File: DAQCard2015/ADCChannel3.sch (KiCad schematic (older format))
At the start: 21 parts, among them U8 THS4524IDBTR, U9 AD9219

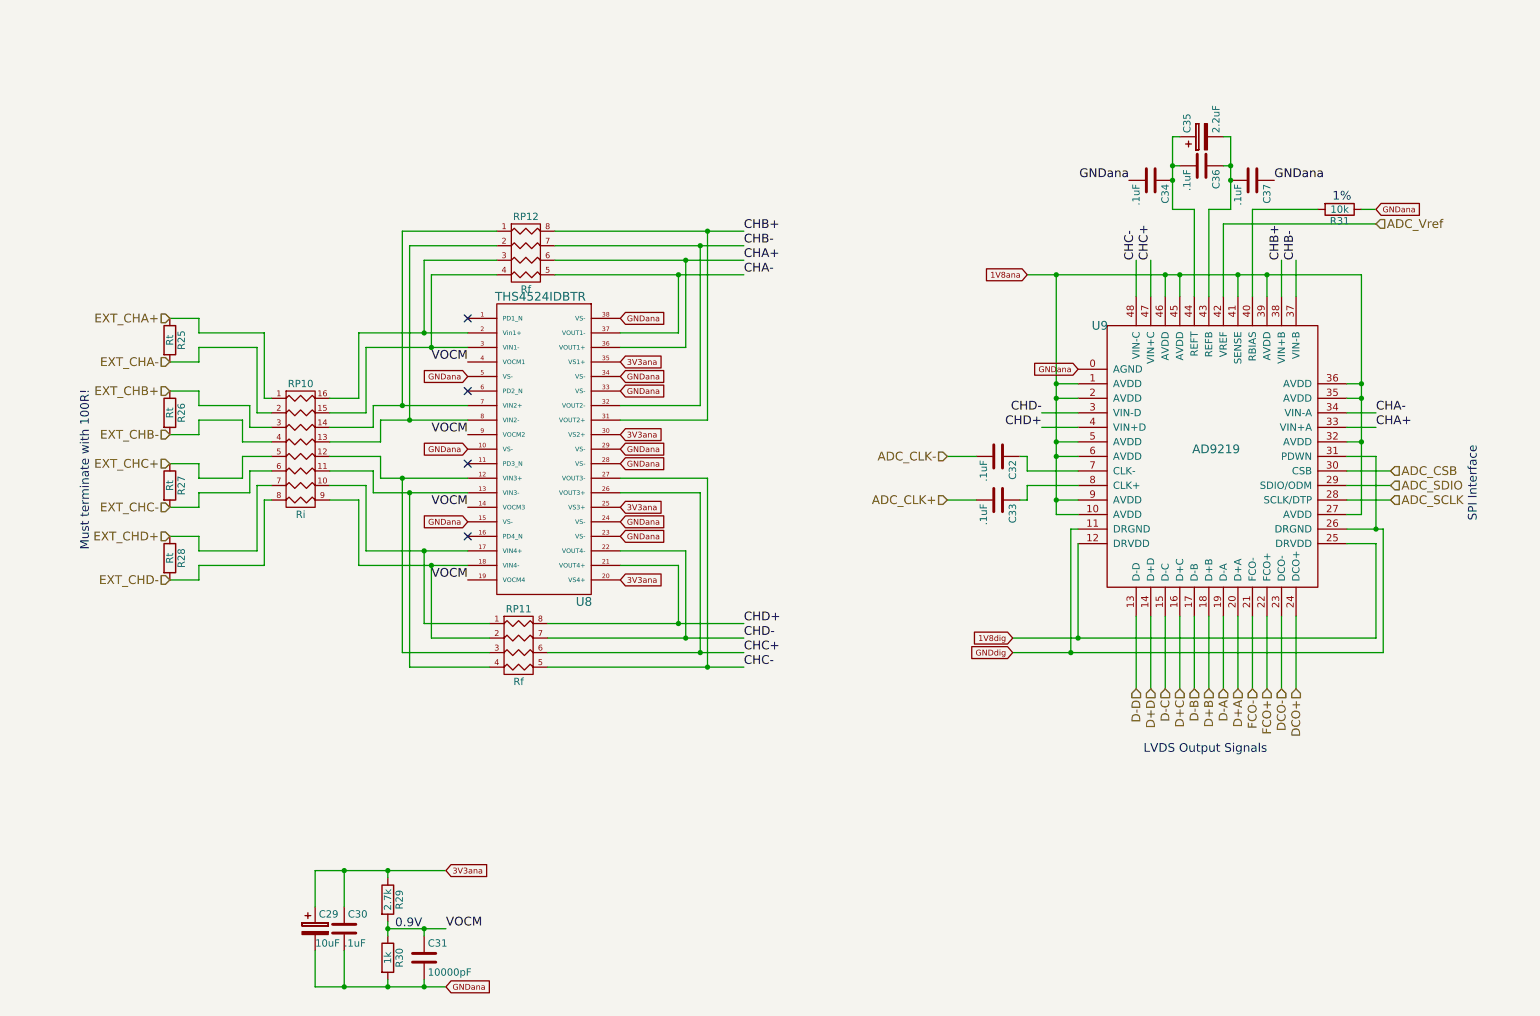
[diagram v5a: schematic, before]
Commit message: propogate previous changes to other channels and schematic
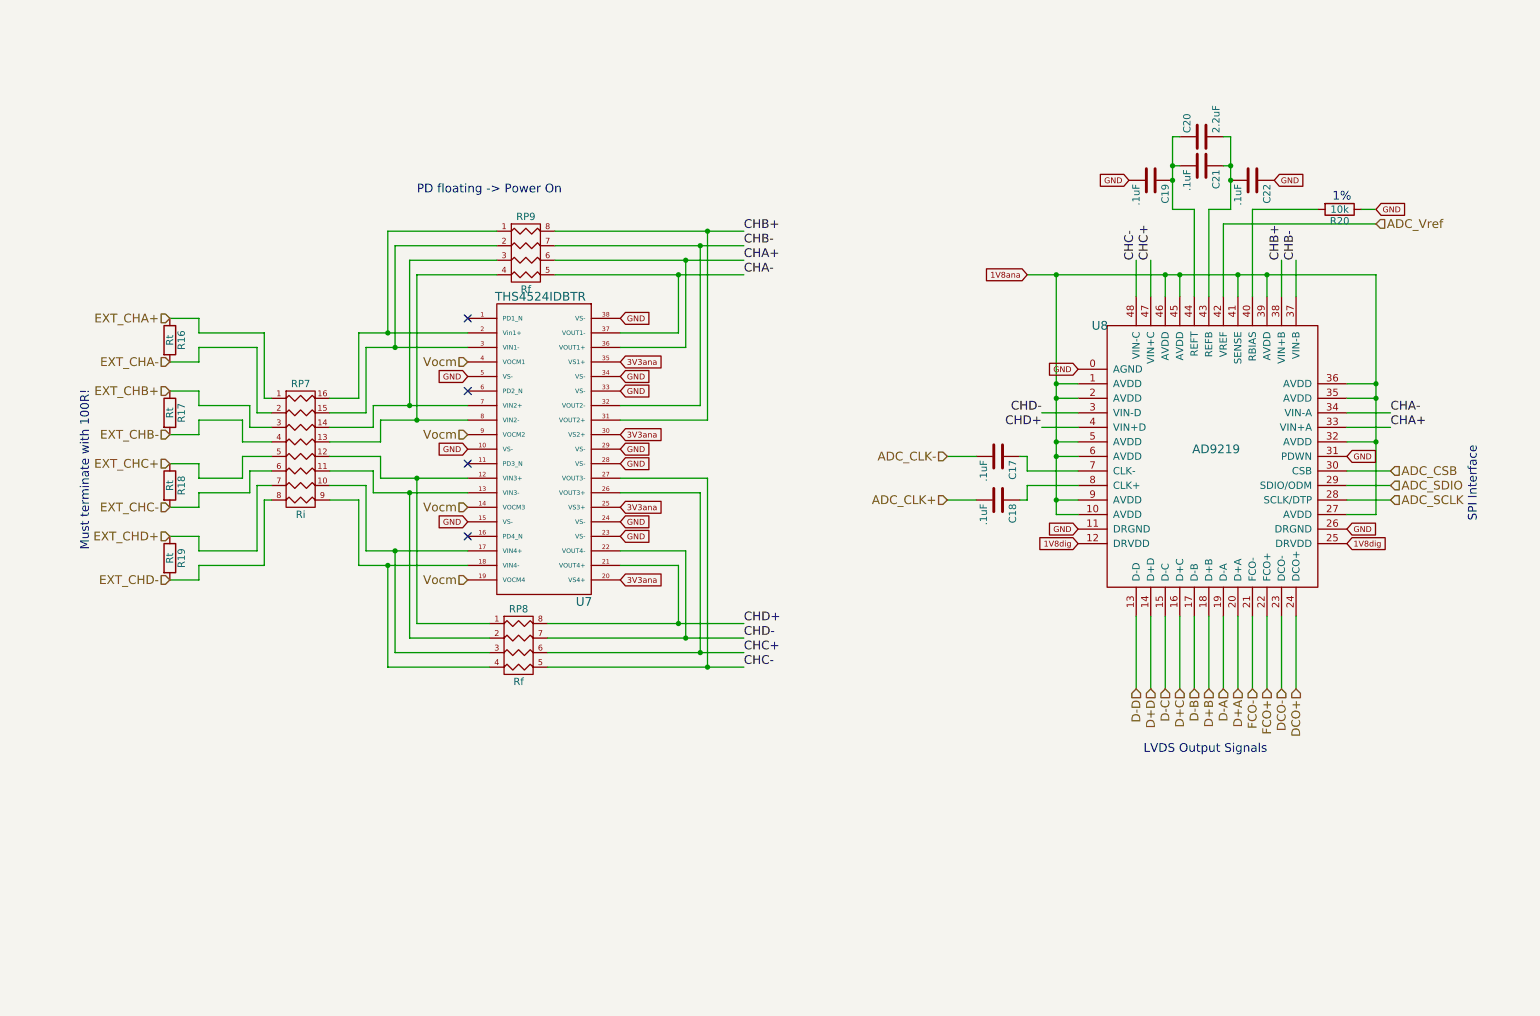
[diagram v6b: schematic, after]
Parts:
- removed C29: 10uF, Capacitors_SMD:C_0805, symbol CP
- removed C30, C32, C33, C34, C36, C37: .1uF, Capacitors_SMD:C_0603, symbol C
- removed C31: 10000pF, Capacitors_SMD:C_0603, symbol C
- removed C35: 2.2uF, Capacitors_SMD:C_0805, symbol CP
- removed R25, R26, R27, R28: Rt, Resistors_SMD:R_0603, symbol R
- removed R29: 2.7k, Resistors_SMD:R_0603, symbol R
- removed R30: 1k, Resistors_SMD:R_0603, symbol R
- removed R31: 10k, Resistors_SMD:R_0603, symbol R
- removed RP10: Ri, extras:R8_MNR18, symbol R_PACK8
- removed RP11, RP12: Rf, extras:R4-MNR04, symbol R_PACK4
- removed U8: THS4524IDBTR, Housings_SSOP:TSSOP-38_4.4x9.7mm_Pitch0.5mm, symbol THS4524IDBTR
- removed U9: AD9219, SMD_Packages:QFN-48-1EP, symbol AD9219
- added C17, C18, C19, C21, C22: .1uF, Capacitors_SMD:C_0603, symbol C
- added C20: 2.2uF, Capacitors_SMD:C_0805, symbol C
- added R16, R17, R18, R19: Rt, Resistors_SMD:R_0603, symbol R
- added R20: 10k, Resistors_SMD:R_0603, symbol R
- added RP7: Ri, extras:R8_MNR18, symbol R_PACK8
- added RP8, RP9: Rf, extras:R4-MNR04, symbol R_PACK4
- added U7: THS4524IDBTR, Housings_SSOP:TSSOP-38_4.4x9.7mm_Pitch0.5mm, symbol THS4524IDBTR
- added U8: AD9219, extras:QFN-48-1EP, symbol AD9219
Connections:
- net 1V8ana: now also U8.1 (AVDD), U8.10 (AVDD), U8.2 (AVDD), U8.27 (AVDD), U8.32 (AVDD), U8.35 (AVDD), U8.36 (AVDD), U8.39 (AVDD), U8.41 (SENSE), U8.45 (AVDD), U8.46 (AVDD), U8.5 (AVDD), U8.6 (AVDD), U8.9 (AVDD)
- net 1V8dig: now also U8.12 (DRVDD), U8.25 (DRVDD)
- net 3V3ana: now also U7.20 (VS4+), U7.25 (VS3+), U7.30 (VS2+), U7.35 (VS1+)
- net ADC_CLK+: now also C18.2
- net ADC_CLK-: now also C17.2
- net ADC_CSB: now also U8.30 (CSB)
- net ADC_SCLK: now also U8.28 (SCLK/DTP)
- net ADC_SDIO: now also U8.29 (SDIO/ODM)
- net ADC_Vref: now also U8.42 (VREF)
- net CHA+: now also RP9.6 (R3), U7.36 (VOUT1+), U8.33 (VIN+A)
- net CHA-: now also RP9.5 (R4), U7.37 (VOUT1-), U8.34 (VIN-A)
- net CHB+: now also RP9.8 (R1), U7.31 (VOUT2+), U8.38 (VIN+B)
- net CHB-: now also RP9.7 (R2), U7.32 (VOUT2-), U8.37 (VIN-B)
- net CHC+: now also RP8.6 (R3), U7.26 (VOUT3+), U8.47 (VIN+C)
- net CHC-: now also RP8.5 (R4), U7.27 (VOUT3-), U8.48 (VIN-C)
- net CHD+: now also RP8.8 (R1), U7.21 (VOUT4+), U8.4 (VIN+D)
- net CHD-: now also RP8.7 (R2), U7.22 (VOUT4-), U8.3 (VIN-D)
- net D+A: now also U8.20 (D+A)
- net D+B: now also U8.18 (D+B)
- net D+C: now also U8.16 (D+C)
- net D+D: now also U8.14 (D+D)
- net D-A: now also U8.19 (D-A)
- net D-B: now also U8.17 (D-B)
- net D-C: now also U8.15 (D-C)
- net D-D: now also U8.13 (D-D)
- net DCO+: now also U8.24 (DCO+)
- net DCO-: now also U8.23 (DCO-)
- net EXT_CHA+: now also R16.1, RP7.1 (P1)
- net EXT_CHA-: now also R16.2, RP7.2 (P2)
- net EXT_CHB+: now also R17.1, RP7.3 (P3)
- net EXT_CHB-: now also R17.2, RP7.4 (P4)
- net EXT_CHC+: now also R18.1, RP7.5 (P5)
- net EXT_CHC-: now also R18.2, RP7.6 (P6)
- net EXT_CHD+: now also R19.1, RP7.7 (P7)
- net EXT_CHD-: now also R19.2, RP7.8 (P8)
- net FCO+: now also U8.22 (FCO+)
- net FCO-: now also U8.21 (FCO-)
- new net: C20.2, C21.1, C22.2, U8.43 (REFB)
- new net: C18.1, U8.8 (CLK+)
- new net: RP7.16 (R1), RP9.1 (P1), U7.2 (Vin1+)
- new net: RP7.15 (R2), RP9.2 (P2), U7.3 (VIN1-)
- new net: RP7.14 (R3), RP9.3 (P3), U7.7 (VIN2+)
- new net: RP7.13 (R4), RP9.4 (P4), U7.8 (VIN2-)
- new net: R20.2, U8.40 (RBIAS)
- new net: C19.1, C20.1, C21.2, U8.44 (REFT)
- new net: C17.1, U8.7 (CLK-)
- new net: RP7.12 (R5), RP8.1 (P1), U7.12 (VIN3+)
- new net: RP7.11 (R6), RP8.2 (P2), U7.13 (VIN3-)
- new net: RP7.10 (R7), RP8.3 (P3), U7.17 (VIN4+)
- new net: RP7.9 (R8), RP8.4 (P4), U7.18 (VIN4-)
- new net GND: C19.2, C22.1, R20.1, U7.10 (VS-), U7.15 (VS-), U7.23 (VS-), U7.24 (VS-), U7.28 (VS-), U7.29 (VS-), U7.33 (VS-), U7.34 (VS-), U7.38 (VS-), U7.5 (VS-), U8.0 (AGND), U8.11 (DRGND), U8.26 (DRGND), U8.31 (PDWN)
- new net Vocm: U7.14 (VOCM3), U7.19 (VOCM4), U7.4 (VOCM1), U7.9 (VOCM2)
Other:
- note added: "PD floating -> Power On"
- note removed: "0.9V"

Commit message: Various updates to DAQ board focusing on power system
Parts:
- U7: footprint Housings_SSOP:TSSOP-38_4.4x9.7mm_Pitch0.5mm -> extras:TSSOP-38_4.4x9.7mm_Pitch0.5mm
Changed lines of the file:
@@
 F 0 "U7" H 4700 2750 60  0000 C CNN
 F 1 "THS4524IDBTR" H 4400 4850 60  0000 C CNN
-F 2 "Housings_SSOP:TSSOP-38_4.4x9.7mm_Pitch0.5mm" H 4600 3800 60  0001 C CNN
+F 2 "extras:TSSOP-38_4.4x9.7mm_Pitch0.5mm" H 4600 3800 60  0001 C CNN
 F 3 "" H 4600 3800 60  0000 C CNN
 	1    4400 3700
